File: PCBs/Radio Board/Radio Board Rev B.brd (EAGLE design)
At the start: 95.9 x 90.2 mm, 4 parts

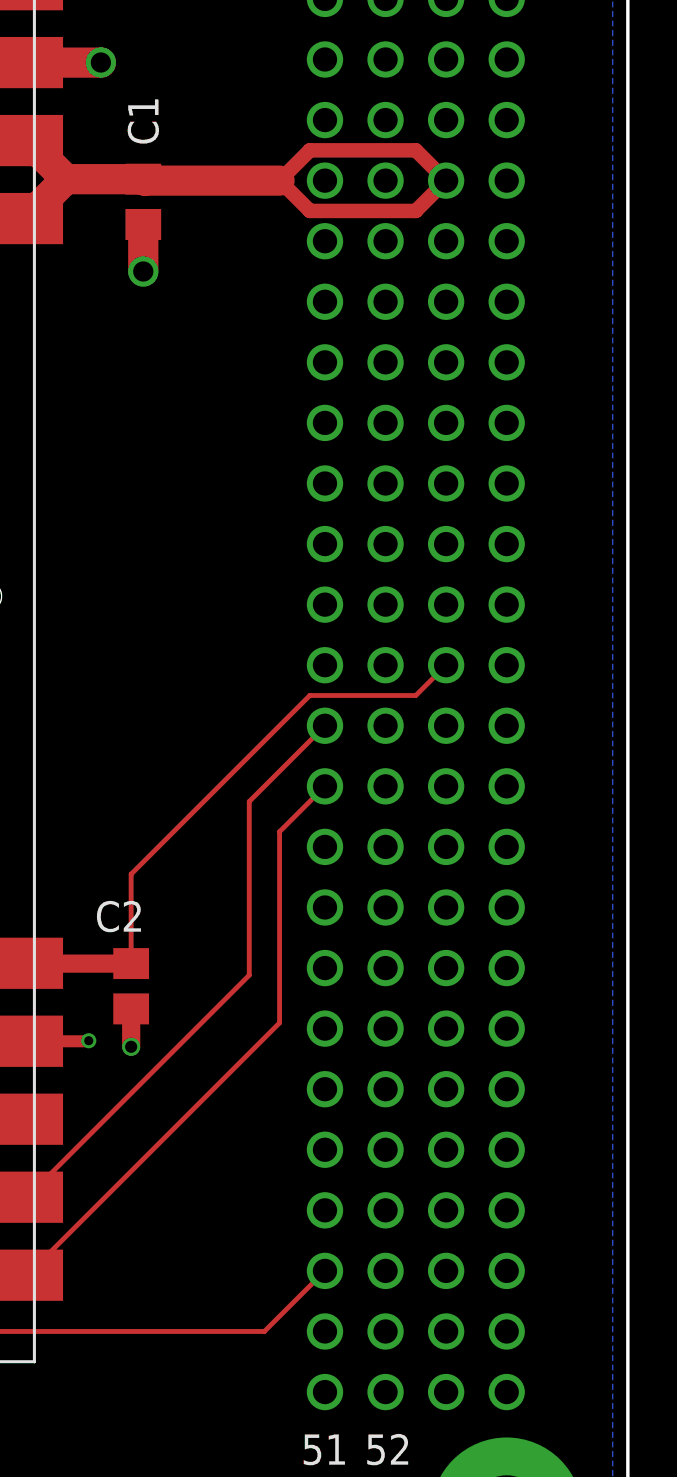
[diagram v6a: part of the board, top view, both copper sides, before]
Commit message: Use different PC104 footprints for each board
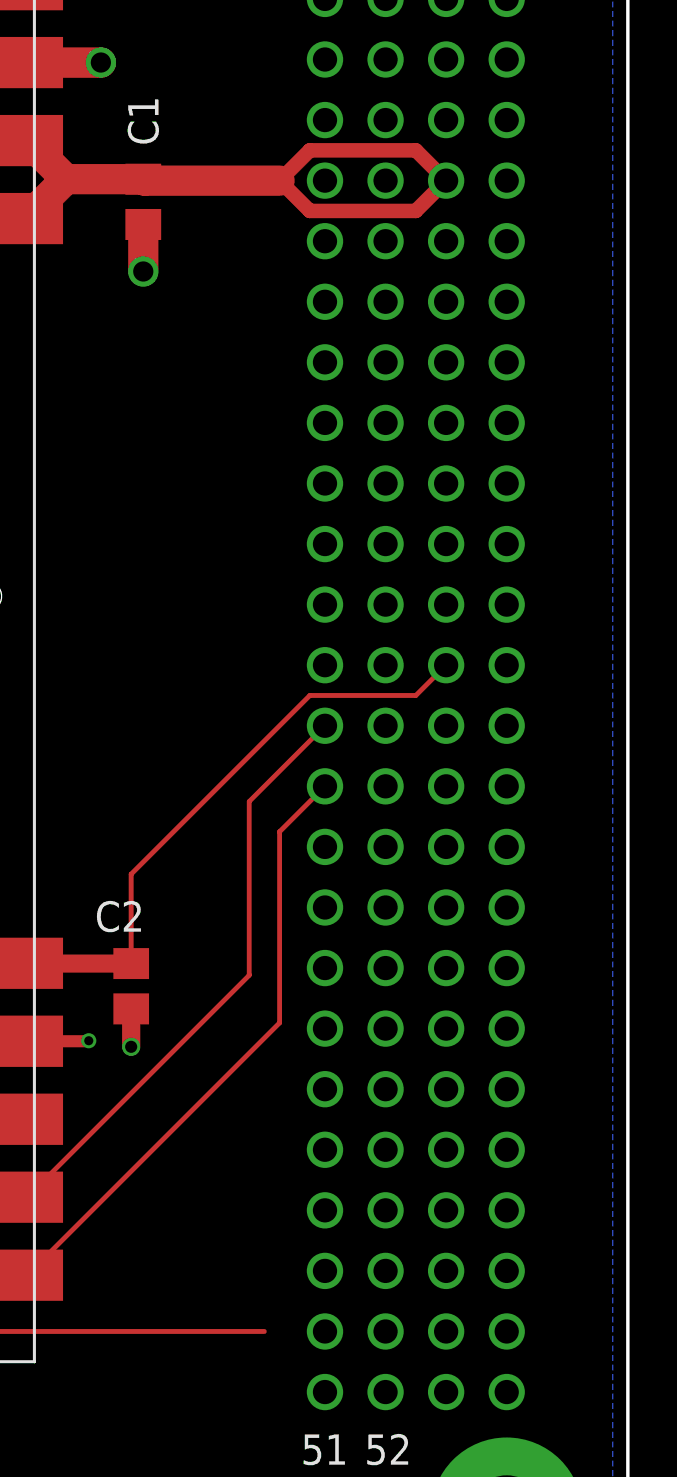
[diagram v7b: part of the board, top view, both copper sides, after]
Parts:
- U$2: value PC104_BOARD -> PC104_RADIO; device Cubesat:PC104_WITH_CSK_HEADER -> Cubesat:PC104_RADIO
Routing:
- net OA_RESET: track 46.8 -> 43.2 mm
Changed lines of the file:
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@@
 </element>
 <element name="U$1" library="Cubesat" package="LI-1" value="LI-1" x="38.1" y="13.97"/>
-<element name="U$2" library="Cubesat" package="PC104_WITH_CSK_HEADER" value="PC104_BOARD" x="0" y="0"/>
+<element name="U$2" library="Cubesat" package="PC104_RADIO" value="PC104_RADIO" x="0" y="0"/>
 </elements>
 <signals>
@@
 <wire x1="75.565" y1="61.661" x2="75.565" y2="59.69" width="1.27" layer="1"/>
 <via x="75.565" y="59.69" extent="1-16" drill="0.846665625"/>
-<contactref element="U$2" pad="61"/>
-<contactref element="U$2" pad="73"/>
-<contactref element="U$2" pad="69"/>
-<contactref element="U$2" pad="81"/>
-<contactref element="U$2" pad="99"/>
-<contactref element="U$2" pad="74"/>
-<contactref element="U$2" pad="66"/>
-<contactref element="U$2" pad="82"/>
-<contactref element="U$2" pad="84"/>
-<contactref element="U$2" pad="100"/>
 <wire x1="70.7" y1="27.41" x2="73.257" y2="27.41" width="0.508" layer="1"/>
 <wire x1="73.257" y1="27.41" x2="73.279" y2="27.432" width="0.508" layer="1"/>
@@
 <wire x1="73.752" y1="71.72" x2="73.787" y2="71.755" width="1.27" layer="1"/>
 <via x="73.787" y="71.755" extent="1-16" drill="0.846665625"/>
+<contactref element="U$2" pad="61"/>
+<contactref element="U$2" pad="74"/>
+<contactref element="U$2" pad="73"/>
+<contactref element="U$2" pad="66"/>
+<contactref element="U$2" pad="69"/>
+<contactref element="U$2" pad="81"/>
+<contactref element="U$2" pad="99"/>
+<contactref element="U$2" pad="82"/>
+<contactref element="U$2" pad="84"/>
+<contactref element="U$2" pad="100"/>
 <wire x1="70.7" y1="68.45" x2="54.4" y2="60.07" width="0" layer="19" extent="1-1"/>
 </signal>
@@
 <wire x1="72.319" y1="63.561" x2="70.7" y2="61.942" width="1.27" layer="1"/>
 <wire x1="70.7" y1="61.942" x2="70.7" y2="61.91" width="1.27" layer="1"/>
+<wire x1="86.995" y1="64.77" x2="82.55" y2="64.77" width="0.6096" layer="1"/>
+<wire x1="86.995" y1="62.23" x2="82.55" y2="62.23" width="0.6096" layer="1"/>
 <contactref element="U$2" pad="63"/>
-<wire x1="86.995" y1="64.77" x2="88.265" y2="63.5" width="0.6096" layer="1"/>
-<wire x1="82.55" y1="64.77" x2="86.995" y2="64.77" width="0.6096" layer="1"/>
-<wire x1="86.995" y1="62.23" x2="88.265" y2="63.5" width="0.6096" layer="1"/>
-<wire x1="82.55" y1="62.23" x2="86.995" y2="62.23" width="0.6096" layer="1"/>
+<wire x1="88.265" y1="63.5" x2="86.995" y2="64.77" width="0.6096" layer="1"/>
+<wire x1="88.265" y1="63.5" x2="86.995" y2="62.23" width="0.6096" layer="1"/>
 </signal>
 <signal name="LITHIUM_TX">
 <contactref element="U$1" pad="TX_UART"/>
+<wire x1="81.28" y1="28.18" x2="70.7" y2="17.6" width="0.2032" layer="1"/>
+<wire x1="81.28" y1="36.195" x2="81.28" y2="28.18" width="0.2032" layer="1"/>
 <contactref element="U$2" pad="31"/>
 <wire x1="83.185" y1="38.1" x2="81.28" y2="36.195" width="0.2032" layer="1"/>
-<wire x1="81.28" y1="28.18" x2="70.7" y2="17.6" width="0.2032" layer="1"/>
-<wire x1="81.28" y1="36.195" x2="81.28" y2="28.18" width="0.2032" layer="1"/>
 </signal>
 <signal name="LITHIUM_RX">
 <contactref element="U$1" pad="RX_UART"/>
+<wire x1="80.01" y1="37.465" x2="80.01" y2="30.18" width="0.2032" layer="1"/>
+<wire x1="80.01" y1="30.18" x2="70.7" y2="20.87" width="0.2032" layer="1"/>
 <contactref element="U$2" pad="29"/>
 <wire x1="83.185" y1="40.64" x2="80.01" y2="37.465" width="0.2032" layer="1"/>
-<wire x1="80.01" y1="37.465" x2="80.01" y2="30.18" width="0.2032" layer="1"/>
-<wire x1="80.01" y1="30.18" x2="70.7" y2="20.87" width="0.2032" layer="1"/>
 </signal>
 <signal name="3V3">
 <contactref element="C2" pad="1"/>
 <contactref element="U$1" pad="3.3V"/>
-<contactref element="U$2" pad="79"/>
 <wire x1="75.057" y1="30.668" x2="70.712" y2="30.668" width="0.762" layer="1"/>
 <wire x1="70.712" y1="30.668" x2="70.7" y2="30.68" width="0.762" layer="1"/>
-<wire x1="88.265" y1="43.18" x2="86.995" y2="41.91" width="0.2032" layer="1"/>
 <wire x1="82.55" y1="41.91" x2="75.057" y2="34.417" width="0.2032" layer="1"/>
 <wire x1="75.057" y1="34.417" x2="75.057" y2="30.668" width="0.2032" layer="1"/>
 <wire x1="86.995" y1="41.91" x2="82.55" y2="41.91" width="0.2032" layer="1"/>
+<contactref element="U$2" pad="79"/>
+<wire x1="88.265" y1="43.18" x2="86.995" y2="41.91" width="0.2032" layer="1"/>
 </signal>
 <signal name="OA_RESET">
 <contactref element="U$1" pad="CONFIG1"/>
+<wire x1="38.4" y1="17.6" x2="40.76" y2="15.24" width="0.2032" layer="1"/>
+<wire x1="40.76" y1="15.24" x2="80.645" y2="15.24" width="0.2032" layer="1"/>
 <contactref element="U$2" pad="47"/>
-<wire x1="38.4" y1="17.6" x2="40.76" y2="15.24" width="0.2032" layer="1"/>
-<wire x1="80.645" y1="15.24" x2="83.185" y2="17.78" width="0.2032" layer="1"/>
-<wire x1="40.76" y1="15.24" x2="80.645" y2="15.24" width="0.2032" layer="1"/>
+<wire x1="80.645" y1="15.24" x2="83.185" y2="17.78" width="0" layer="19" extent="1-1"/>
 </signal>
 </signals>
